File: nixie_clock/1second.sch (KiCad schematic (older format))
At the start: 8 parts

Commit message: minor cleanups
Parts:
- removed C?: 0.1uF, symbol C
- removed P?: CONN_01X03, symbol CONN_01X03
- removed P?: CONN_01X02, symbol CONN_01X02
- removed R?: 33K, symbol R
- removed R?: 1K, symbol R
- removed U?: 4518, symbol 4518
- removed U?: K155ID1, symbol K155ID1
- removed U?: IN-12, symbol IN-12
- added C6: 0.1uF, symbol C
- added P12: CONN_01X03, symbol CONN_01X03
- added P13: CONN_01X02, symbol CONN_01X02
- added R11: 1K, symbol R
- added R12: 33K, symbol R
- added U12: 4518, symbol 4518
- added U16: K155ID1, symbol K155ID1
- added U17: IN-12, symbol IN-12
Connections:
- net +220V: now also R12.2
- net +5V: now also R11.1, U12.16 (VDD), U16.5 (VCC)
- net CLK_IN: now also P12.3 (P3)
- net CLK_OUT: now also U12.14 (Q4), U16.4 (INPUT_D)
- net GND: now also C6.2, P13.2 (P2), U12.15 (Reset), U12.8 (VSS), U12.9 (CK), U16.12 (GND)
- new net: P12.2 (P2), U12.10 (Enable)
- new net: U12.11 (Q1), U16.3 (INPUT_A)
- new net: U12.12 (Q2), U16.6 (INPUT_B)
- new net: U12.13 (Q3), U16.7 (INPUT_C)
- new net: U16.1 (OUT_8), U17.4 (8-KATOD)
- new net: U16.10 (OUT_7), U17.5 (7-KATOD)
- new net: U16.11 (OUT_6), U17.6 (6-KATOD)
- new net: U16.13 (OUT_4), U17.8 (4-KATOD)
- new net: U16.14 (OUT_5), U17.7 (5-KATOD)
- new net: U16.15 (OUT_1), U17.11 (1-KATOD)
- new net: U16.16 (OUT_0), U17.2 (0-KATOD)
- new net: U16.2 (OUT_9), U17.3 (9-KATOD)
- new net: U16.8 (OUT_2), U17.10 (2-KATOD)
- new net: U16.9 (OUT_3), U17.9 (3-KATOD)
- new net: R12.1, U17.1 (ANOD)
- new net: C6.1, P12.1 (P1), P13.1 (P1), R11.2
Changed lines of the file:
@@
 $EndDescr
 $Comp
-L 4518 U?
-U 1 1 590D5881
+L 4518 U12
+U 2 1 591359E9
 P 3900 2950
-F 0 "U?" H 3950 3400 50  0000 C CNN
+F 0 "U12" H 3950 3400 50  0000 C CNN
 F 1 "4518" H 4100 2600 50  0000 C CNN
 F 2 "" H 3900 2950 60  0001 C CNN
 F 3 "" H 3900 2950 60  0001 C CNN
-	1    3900 2950
-	1    0    0    -1
-$EndComp
-$Comp
-L K155ID1 U?
-U 1 1 590D5D46
+	2    3900 2950
+	1    0    0    -1
+$EndComp
+$Comp
+L K155ID1 U16
+U 1 1 591359EE
 P 6800 3350
-F 0 "U?" H 6800 3200 60  0000 C CNN
+F 0 "U16" H 6800 3200 60  0000 C CNN
 F 1 "K155ID1" H 6850 3300 60  0000 C CNN
 F 2 "" H 6800 3350 60  0001 C CNN
@@
 	5050 3500 5050 3450
 $Comp
-L IN-12 U?
-U 1 1 590D638A
+L IN-12 U17
+U 1 1 591359F5
 P 9000 4750
-F 0 "U?" H 9000 4650 60  0000 C CNN
+F 0 "U17" H 9000 4650 60  0000 C CNN
 F 1 "IN-12" H 9000 4750 60  0000 C CNN
 F 2 "" H 9000 4750 60  0001 C CNN
@@
 $EndComp
 $Comp
-L R R?
-U 1 1 590D63EB
+L R R12
+U 1 1 591359F9
 P 8300 5900
-F 0 "R?" V 8380 5900 50  0000 C CNN
+F 0 "R12" V 8380 5900 50  0000 C CNN
 F 1 "33K" V 8300 5900 50  0000 C CNN
 F 2 "" V 8230 5900 50  0000 C CNN
@@
 NoConn ~ 9000 5750
 $Comp
-L +5V #PWR?
-U 1 1 590D6CDB
+L +5V #PWR090
+U 1 1 591359FF
 P 5700 2950
-F 0 "#PWR?" H 5700 2800 50  0001 C CNN
+F 0 "#PWR090" H 5700 2800 50  0001 C CNN
 F 1 "+5V" H 5700 3090 50  0000 C CNN
 F 2 "" H 5700 2950 50  0000 C CNN
@@
 $EndComp
 $Comp
-L GND #PWR?
-U 1 1 590D6CFB
+L GND #PWR091
+U 1 1 59135A03
 P 7550 3900
-F 0 "#PWR?" H 7550 3650 50  0001 C CNN
+F 0 "#PWR091" H 7550 3650 50  0001 C CNN
 F 1 "GND" H 7550 3750 50  0000 C CNN
 F 2 "" H 7550 3900 50  0000 C CNN
@@
 	7550 3900 7550 3400
 $Comp
-L +5V #PWR?
-U 1 1 590D72A1
-P 4800 1750
-F 0 "#PWR?" H 4800 1600 50  0001 C CNN
-F 1 "+5V" H 4800 1890 50  0000 C CNN
-F 2 "" H 4800 1750 50  0000 C CNN
-F 3 "" H 4800 1750 50  0000 C CNN
-	1    4800 1750
-	1    0    0    -1
-$EndComp
-$Comp
-L VDD #PWR?
-U 1 1 590D72C1
-P 5100 1750
-F 0 "#PWR?" H 5100 1600 50  0001 C CNN
-F 1 "VDD" H 5100 1900 50  0000 C CNN
-F 2 "" H 5100 1750 50  0000 C CNN
-F 3 "" H 5100 1750 50  0000 C CNN
-	1    5100 1750
-	1    0    0    -1
-$EndComp
-$Comp
-L GND #PWR?
-U 1 1 590D72E1
-P 4800 2100
-F 0 "#PWR?" H 4800 1850 50  0001 C CNN
-F 1 "GND" H 4800 1950 50  0000 C CNN
-F 2 "" H 4800 2100 50  0000 C CNN
-F 3 "" H 4800 2100 50  0000 C CNN
-	1    4800 2100
-	1    0    0    -1
-$EndComp
-$Comp
-L VSS #PWR?
-U 1 1 590D7301
-P 5100 2100
-F 0 "#PWR?" H 5100 1950 50  0001 C CNN
-F 1 "VSS" H 5100 2250 50  0000 C CNN
-F 2 "" H 5100 2100 50  0000 C CNN
-F 3 "" H 5100 2100 50  0000 C CNN
-	1    5100 2100
+L +5V #PWR092
+U 1 1 59135A05
+P 4800 1700
+F 0 "#PWR092" H 4800 1550 50  0001 C CNN
+F 1 "+5V" H 4800 1840 50  0000 C CNN
+F 2 "" H 4800 1700 50  0000 C CNN
+F 3 "" H 4800 1700 50  0000 C CNN
+	1    4800 1700
+	1    0    0    -1
+$EndComp
+$Comp
+L VDD #PWR093
+U 1 1 59135A0A
+P 5100 1700
+F 0 "#PWR093" H 5100 1550 50  0001 C CNN
+F 1 "VDD" H 5100 1850 50  0000 C CNN
+F 2 "" H 5100 1700 50  0000 C CNN
+F 3 "" H 5100 1700 50  0000 C CNN
+	1    5100 1700
+	1    0    0    -1
+$EndComp
+$Comp
+L GND #PWR094
+U 1 1 59135A11
+P 4800 2150
+F 0 "#PWR094" H 4800 1900 50  0001 C CNN
+F 1 "GND" H 4800 2000 50  0000 C CNN
+F 2 "" H 4800 2150 50  0000 C CNN
+F 3 "" H 4800 2150 50  0000 C CNN
+	1    4800 2150
+	1    0    0    -1
+$EndComp
+$Comp
+L VSS #PWR095
+U 1 1 59135A16
+P 5100 2050
+F 0 "#PWR095" H 5100 1900 50  0001 C CNN
+F 1 "VSS" H 5100 2200 50  0000 C CNN
+F 2 "" H 5100 2050 50  0000 C CNN
+F 3 "" H 5100 2050 50  0000 C CNN
+	1    5100 2050
 	1    0    0    -1
 $EndComp
@@
 GND
 $Comp
-L +5V #PWR?
-U 1 1 590D7886
-P 2700 1950
-F 0 "#PWR?" H 2700 1800 50  0001 C CNN
-F 1 "+5V" H 2700 2090 50  0000 C CNN
-F 2 "" H 2700 1950 50  0000 C CNN
-F 3 "" H 2700 1950 50  0000 C CNN
-	1    2700 1950
-	1    0    0    -1
-$EndComp
-$Comp
-L GND #PWR?
-U 1 1 590D78A6
-P 2700 2200
-F 0 "#PWR?" H 2700 1950 50  0001 C CNN
-F 1 "GND" H 2700 2050 50  0000 C CNN
-F 2 "" H 2700 2200 50  0000 C CNN
-F 3 "" H 2700 2200 50  0000 C CNN
-	1    2700 2200
+L +5V #PWR096
+U 1 1 59135A1D
+P 2700 1900
+F 0 "#PWR096" H 2700 1750 50  0001 C CNN
+F 1 "+5V" H 2700 2040 50  0000 C CNN
+F 2 "" H 2700 1900 50  0000 C CNN
+F 3 "" H 2700 1900 50  0000 C CNN
+	1    2700 1900
+	1    0    0    -1
+$EndComp
+$Comp
+L GND #PWR097
+U 1 1 59135A1E
+P 2700 2250
+F 0 "#PWR097" H 2700 2000 50  0001 C CNN
+F 1 "GND" H 2700 2100 50  0000 C CNN
+F 2 "" H 2700 2250 50  0000 C CNN
+F 3 "" H 2700 2250 50  0000 C CNN
+	1    2700 2250
 	1    0    0    -1
 $EndComp
@@
 	2600 1450 2700 1450
 $Comp
-L GND #PWR?
-U 1 1 590E0247
+L GND #PWR098
+U 1 1 59135A24
 P 2750 2800
-F 0 "#PWR?" H 2750 2550 50  0001 C CNN
+F 0 "#PWR098" H 2750 2550 50  0001 C CNN
 F 1 "GND" H 2750 2650 50  0000 C CNN
 F 2 "" H 2750 2800 50  0000 C CNN
@@
 	4750 3800 5300 3800
 $Comp
-L CONN_01X03 P?
-U 1 1 590F618F
+L CONN_01X03 P12
+U 1 1 59135A2B
 P 2200 3650
-F 0 "P?" H 2200 3850 50  0000 C CNN
+F 0 "P12" H 2200 3850 50  0000 C CNN
 F 1 "CONN_01X03" V 2300 3650 50  0000 C CNN
 F 2 "" H 2200 3650 50  0000 C CNN
@@
 $EndComp
 $Comp
-L CONN_01X02 P?
-U 1 1 590F61CD
+L CONN_01X02 P13
+U 1 1 59135A2D
 P 2950 3850
-F 0 "P?" H 2950 4000 50  0000 C CNN
+F 0 "P13" H 2950 4000 50  0000 C CNN
 F 1 "CONN_01X02" V 3050 3850 50  0000 C CNN
 F 2 "" H 2950 3850 50  0000 C CNN
@@
 	2200 3000 3300 3000
 $Comp
-L R R?
-U 1 1 590F6393
+L R R11
+U 1 1 59135A35
 P 2450 3250
-F 0 "R?" V 2530 3250 50  0000 C CNN
+F 0 "R11" V 2530 3250 50  0000 C CNN
 F 1 "1K" V 2450 3250 50  0000 C CNN
 F 2 "" V 2380 3250 50  0000 C CNN
@@
 $EndComp
 $Comp
-L +5V #PWR?
+L +5V #PWR099
 U 1 1 590F63C0
 P 2450 2950
-F 0 "#PWR?" H 2450 2800 50  0001 C CNN
+F 0 "#PWR099" H 2450 2800 50  0001 C CNN
 F 1 "+5V" H 2450 3090 50  0000 C CNN
 F 2 "" H 2450 2950 50  0000 C CNN
@@
 $EndComp
 $Comp
-L GND #PWR?
-U 1 1 590F63E6
+L GND #PWR0100
+U 1 1 59135A40
 P 2750 4050
-F 0 "#PWR?" H 2750 3800 50  0001 C CNN
+F 0 "#PWR0100" H 2750 3800 50  0001 C CNN
 F 1 "GND" H 2750 3900 50  0000 C CNN
 F 2 "" H 2750 4050 50  0000 C CNN
@@
 	2450 2950 2450 3100
 $Comp
-L C C?
-U 1 1 590F6DC1
+L C C6
+U 1 1 59135A43
 P 2600 3850
-F 0 "C?" H 2625 3950 50  0000 L CNN
+F 0 "C6" H 2625 3950 50  0000 L CNN
 F 1 "0.1uF" H 2400 3750 50  0000 L CNN
 F 2 "" H 2638 3700 50  0000 C CNN
@@
 Connection ~ 2450 3450
 $Comp
-L +220V #PWR?
-U 1 1 5910CD3A
-P 2700 1450
-F 0 "#PWR?" H 2700 1300 50  0001 C CNN
-F 1 "+220V" H 2700 1590 50  0000 C CNN
-F 2 "" H 2700 1450 50  0000 C CNN
-F 3 "" H 2700 1450 50  0000 C CNN
-	1    2700 1450
-	1    0    0    -1
-$EndComp
-$Comp
-L +220V #PWR?
-U 1 1 5910CDE4
+L +220V #PWR0101
+U 1 1 59135A4A
+P 2700 1400
+F 0 "#PWR0101" H 2700 1250 50  0001 C CNN
+F 1 "+220V" H 2700 1540 50  0000 C CNN
+F 2 "" H 2700 1400 50  0000 C CNN
+F 3 "" H 2700 1400 50  0000 C CNN
+	1    2700 1400
+	1    0    0    -1
+$EndComp
+$Comp
+L +220V #PWR0102
+U 1 1 59135A4B
 P 7850 5850
-F 0 "#PWR?" H 7850 5700 50  0001 C CNN
+F 0 "#PWR0102" H 7850 5700 50  0001 C CNN
 F 1 "+220V" H 7850 5990 50  0000 C CNN
 F 2 "" H 7850 5850 50  0000 C CNN
@@
 	5300 3800 5300 3300
 Connection ~ 5300 3300
+Wire Wire Line
+	4800 1750 4800 1700
+Wire Wire Line
+	5100 1750 5100 1700
+Wire Wire Line
+	5100 2100 5100 2050
+Wire Wire Line
+	4800 2150 4800 2100
+Wire Wire Line
+	2700 1450 2700 1400
+Wire Wire Line
+	2700 1950 2700 1900
+Wire Wire Line
+	2700 2250 2700 2200
 $EndSCHEMATC

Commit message: Footprint associations
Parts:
- C6: footprint (none) -> Capacitors_THT:C_Axial_L5.1mm_D3.1mm_P7.50mm_Horizontal
- P12: footprint (none) -> Pin_Headers:Pin_Header_Straight_1x03_Pitch2.54mm
- P13: footprint (none) -> Pin_Headers:Pin_Header_Straight_1x02_Pitch2.54mm
- R11: footprint (none) -> Resistors_THT:R_Axial_DIN0207_L6.3mm_D2.5mm_P10.16mm_Horizontal
- R12: footprint (none) -> hv:R_Axial_DIN0309_L9.0mm_D3.2mm_P12.70mm_Horizontal_Thick
- U12, U16: footprint (none) -> Housings_DIP:DIP-16_W7.62mm
- U17: footprint (none) -> hv:IN12
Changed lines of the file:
@@
 F 0 "U12" H 3950 3400 50  0000 C CNN
 F 1 "4518" H 4100 2600 50  0000 C CNN
-F 2 "" H 3900 2950 60  0001 C CNN
+F 2 "Housings_DIP:DIP-16_W7.62mm" H 3900 2950 60  0001 C CNN
 F 3 "" H 3900 2950 60  0001 C CNN
 	2    3900 2950
@@
 F 0 "U16" H 6800 3200 60  0000 C CNN
 F 1 "K155ID1" H 6850 3300 60  0000 C CNN
-F 2 "" H 6800 3350 60  0001 C CNN
+F 2 "Housings_DIP:DIP-16_W7.62mm" H 6800 3350 60  0001 C CNN
 F 3 "" H 6800 3350 60  0001 C CNN
 	1    6800 3350
@@
 F 0 "U17" H 9000 4650 60  0000 C CNN
 F 1 "IN-12" H 9000 4750 60  0000 C CNN
-F 2 "" H 9000 4750 60  0001 C CNN
+F 2 "hv:IN12" H 9000 4750 60  0001 C CNN
 F 3 "" H 9000 4750 60  0001 C CNN
 	1    9000 4750
@@
 F 0 "R12" V 8380 5900 50  0000 C CNN
 F 1 "33K" V 8300 5900 50  0000 C CNN
-F 2 "" V 8230 5900 50  0000 C CNN
+F 2 "hv:R_Axial_DIN0309_L9.0mm_D3.2mm_P12.70mm_Horizontal_Thick" V 8230 5900 50  0001 C CNN
 F 3 "" H 8300 5900 50  0000 C CNN
 	1    8300 5900
@@
 F 0 "P12" H 2200 3850 50  0000 C CNN
 F 1 "CONN_01X03" V 2300 3650 50  0000 C CNN
-F 2 "" H 2200 3650 50  0000 C CNN
+F 2 "Pin_Headers:Pin_Header_Straight_1x03_Pitch2.54mm" H 2200 3650 50  0001 C CNN
 F 3 "" H 2200 3650 50  0000 C CNN
 	1    2200 3650
@@
 F 0 "P13" H 2950 4000 50  0000 C CNN
 F 1 "CONN_01X02" V 3050 3850 50  0000 C CNN
-F 2 "" H 2950 3850 50  0000 C CNN
+F 2 "Pin_Headers:Pin_Header_Straight_1x02_Pitch2.54mm" H 2950 3850 50  0001 C CNN
 F 3 "" H 2950 3850 50  0000 C CNN
 	1    2950 3850
@@
 F 0 "R11" V 2530 3250 50  0000 C CNN
 F 1 "1K" V 2450 3250 50  0000 C CNN
-F 2 "" V 2380 3250 50  0000 C CNN
+F 2 "Resistors_THT:R_Axial_DIN0207_L6.3mm_D2.5mm_P10.16mm_Horizontal" V 2380 3250 50  0001 C CNN
 F 3 "" H 2450 3250 50  0000 C CNN
 	1    2450 3250
@@
 F 0 "C6" H 2625 3950 50  0000 L CNN
 F 1 "0.1uF" H 2400 3750 50  0000 L CNN
-F 2 "" H 2638 3700 50  0000 C CNN
+F 2 "Capacitors_THT:C_Axial_L5.1mm_D3.1mm_P7.50mm_Horizontal" H 2638 3700 50  0001 C CNN
 F 3 "" H 2600 3850 50  0000 C CNN
 	1    2600 3850

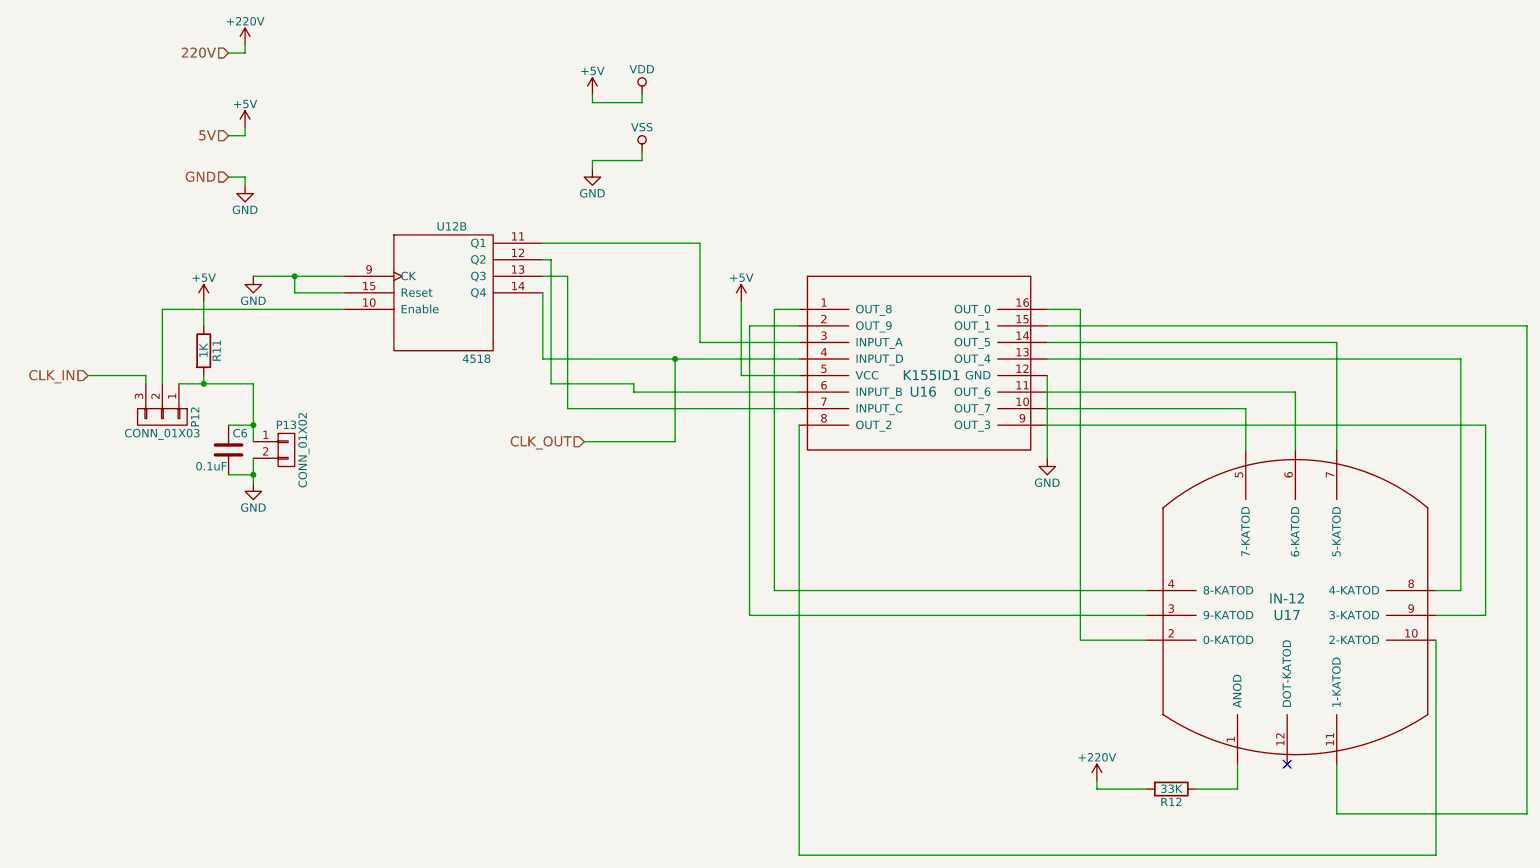
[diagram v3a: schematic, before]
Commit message: Overhaul of clock board. Fixed hour digits, added more noise immunity, reduced height
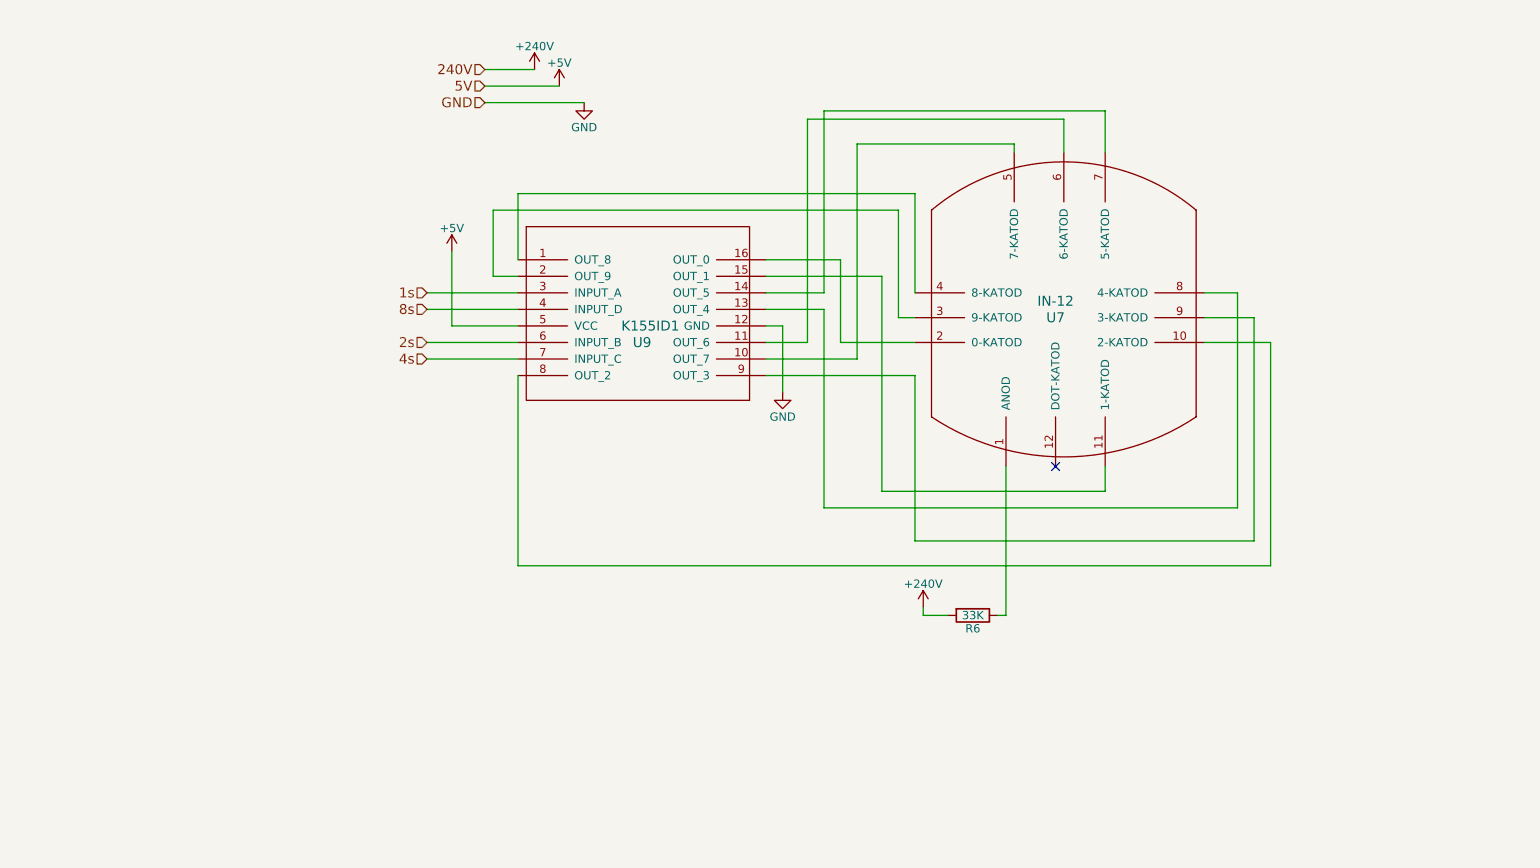
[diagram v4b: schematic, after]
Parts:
- removed C6: 0.1uF, Capacitors_THT:C_Axial_L5.1mm_D3.1mm_P7.50mm_Horizontal, symbol C
- removed P12: CONN_01X03, Pin_Headers:Pin_Header_Straight_1x03_Pitch2.54mm, symbol CONN_01X03
- removed P13: CONN_01X02, Pin_Headers:Pin_Header_Straight_1x02_Pitch2.54mm, symbol CONN_01X02
- removed R11: 1K, Resistors_THT:R_Axial_DIN0207_L6.3mm_D2.5mm_P10.16mm_Horizontal, symbol R
- removed R12: 33K, hv:R_Axial_DIN0309_L9.0mm_D3.2mm_P12.70mm_Horizontal_Thick, symbol R
- removed U12: 4518, Housings_DIP:DIP-16_W7.62mm, symbol 4518
- removed U16: K155ID1, Housings_DIP:DIP-16_W7.62mm, symbol K155ID1
- removed U17: IN-12, hv:IN12, symbol IN-12
- added R6: 33K, hv:R_Axial_DIN0309_L9.0mm_D3.2mm_P12.70mm_Horizontal_Thick, symbol R
- added U7: IN-12, hv:IN12, symbol IN-12
- added U9: K155ID1, Housings_DIP:DIP-16_W7.62mm, symbol K155ID1
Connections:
- net +5V: now also U9.5 (VCC)
- net GND: now also U9.12 (GND)
- new net: R6.1, U7.1 (ANOD)
- new net: U7.10 (2-KATOD), U9.8 (OUT_2)
- new net: U7.11 (1-KATOD), U9.15 (OUT_1)
- new net: U7.2 (0-KATOD), U9.16 (OUT_0)
- new net: U7.3 (9-KATOD), U9.2 (OUT_9)
- new net: U7.4 (8-KATOD), U9.1 (OUT_8)
- new net: U7.5 (7-KATOD), U9.10 (OUT_7)
- new net: U7.6 (6-KATOD), U9.11 (OUT_6)
- new net: U7.7 (5-KATOD), U9.14 (OUT_5)
- new net: U7.8 (4-KATOD), U9.13 (OUT_4)
- new net: U7.9 (3-KATOD), U9.9 (OUT_3)
- new net +240V: R6.2
- new net 1s: U9.3 (INPUT_A)
- new net 2s: U9.6 (INPUT_B)
- new net 4s: U9.7 (INPUT_C)
- new net 8s: U9.4 (INPUT_D)
